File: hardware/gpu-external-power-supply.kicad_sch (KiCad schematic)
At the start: 0 parts

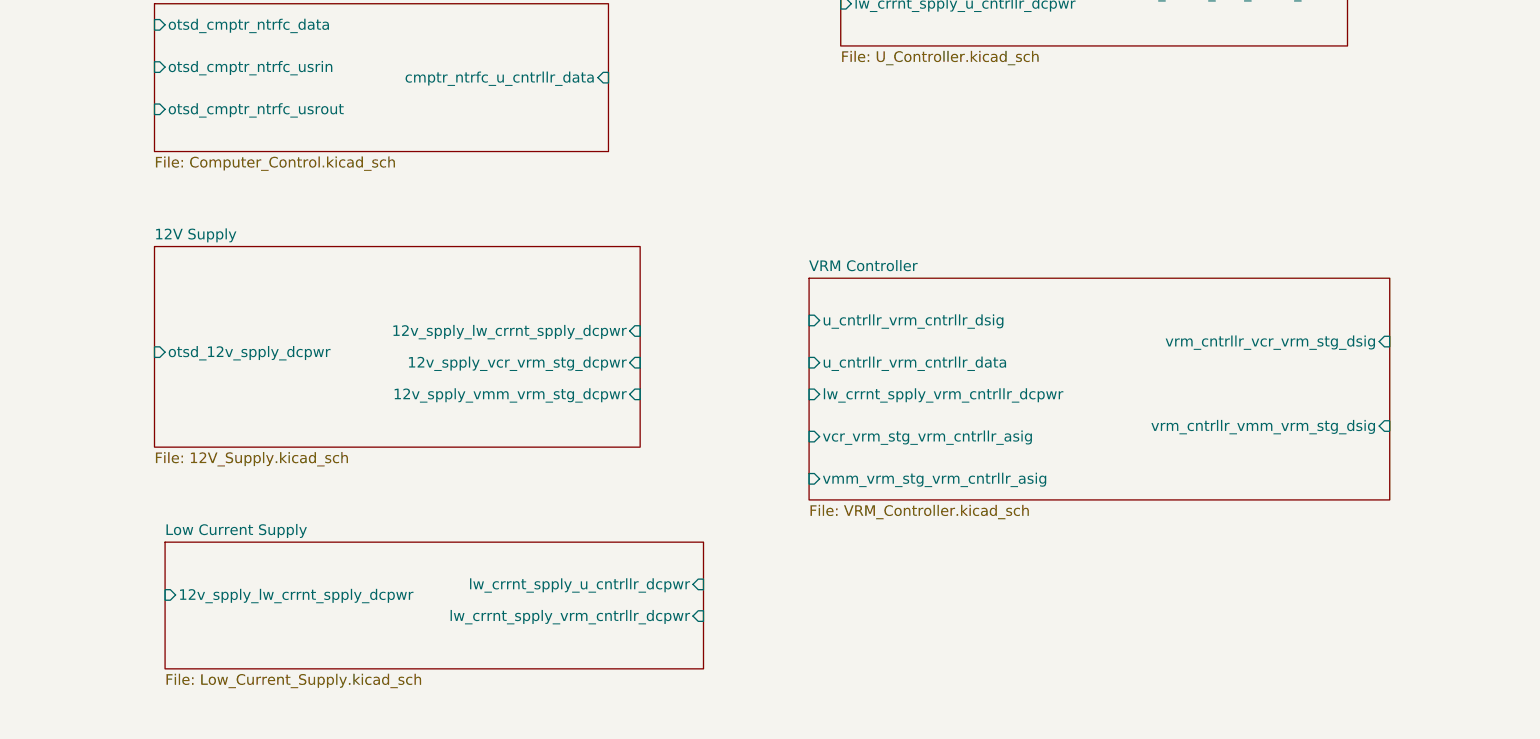
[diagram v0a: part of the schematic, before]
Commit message: refactor(schematic): Update VRM Controller Pins
Updated the VRM controller pinout on the main schematic
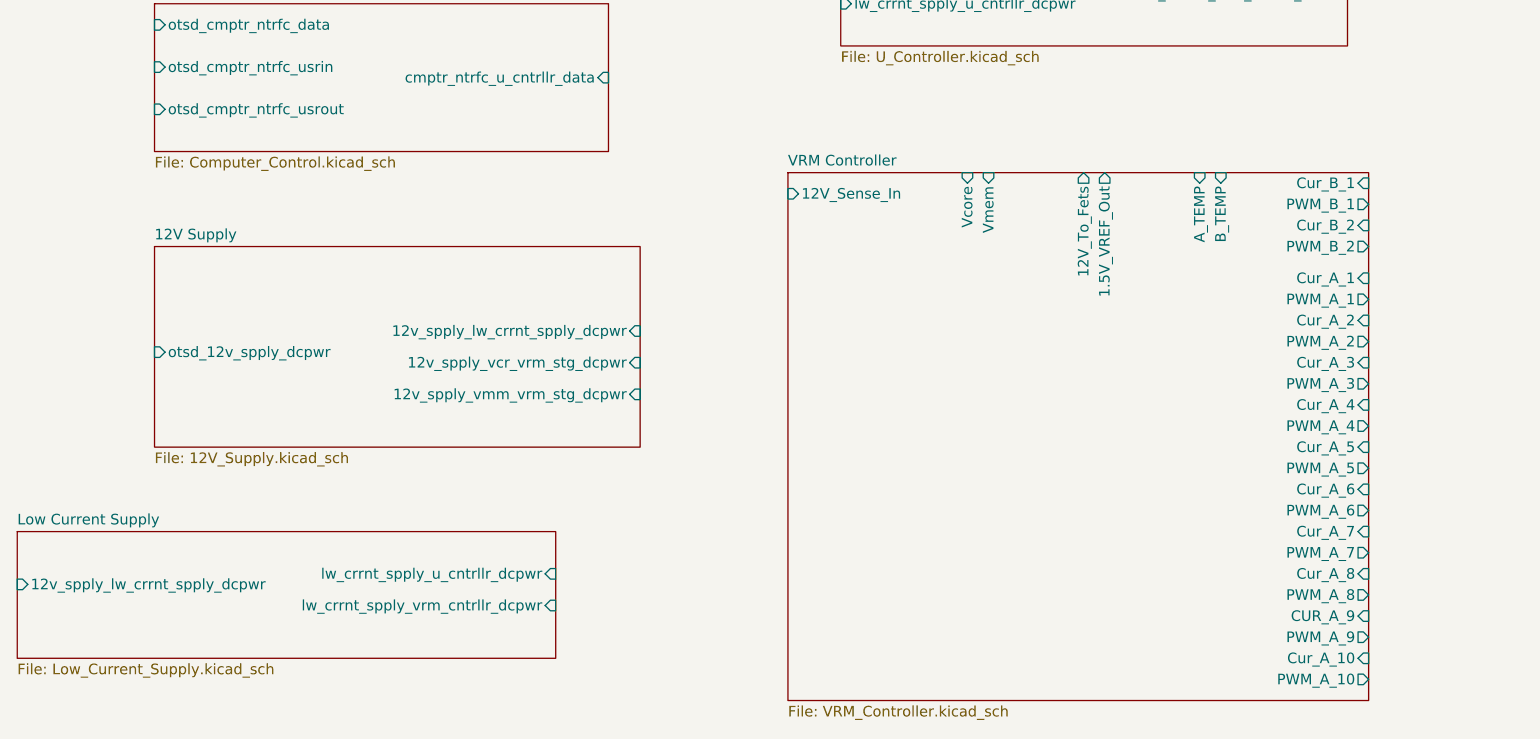
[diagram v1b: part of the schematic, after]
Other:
- sheet VRM Controller ports: added 1.5V_VREF_Out, 12V_Sense_In, 12V_To_Fets, A_TEMP, B_TEMP, CUR_A_9, Cur_A_1, Cur_A_10, Cur_A_2, Cur_A_3, Cur_A_4, Cur_A_5, Cur_A_6, Cur_A_7, Cur_A_8, Cur_B_1, Cur_B_2, PWM_A_1, PWM_A_10, PWM_A_2, PWM_A_3, PWM_A_4, PWM_A_5, PWM_A_6, PWM_A_7, PWM_A_8, PWM_A_9, PWM_B_1, PWM_B_2, Vcore, Vmem; removed lw_crrnt_spply_vrm_cntrllr_dcpwr, u_cntrllr_vrm_cntrllr_data, u_cntrllr_vrm_cntrllr_dsig, vcr_vrm_stg_vrm_cntrllr_asig, vmm_vrm_stg_vrm_cntrllr_asig, vrm_cntrllr_vcr_vrm_stg_dsig, vrm_cntrllr_vmm_vrm_stg_dsig

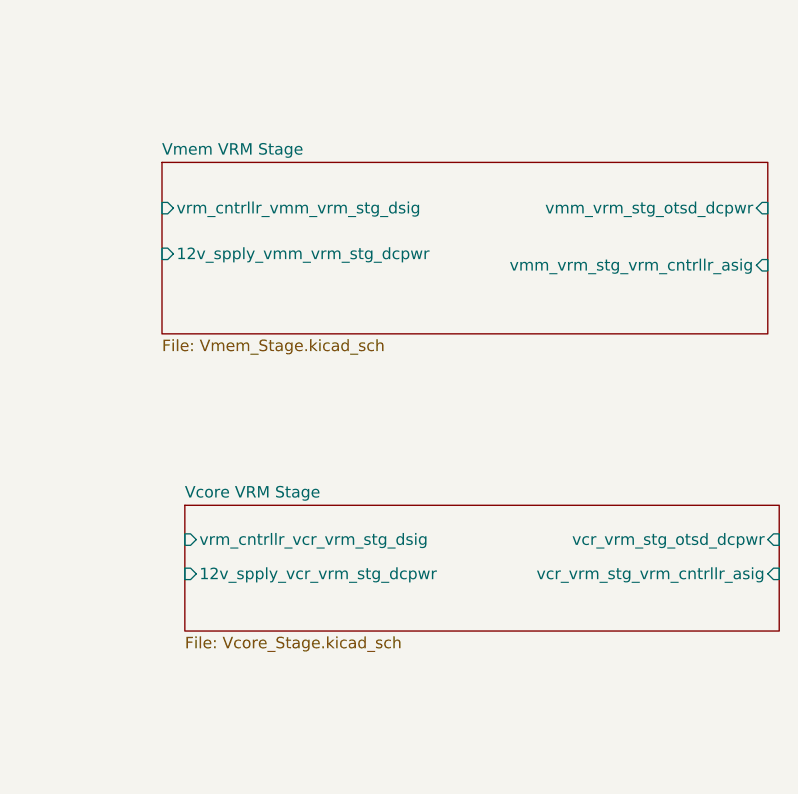
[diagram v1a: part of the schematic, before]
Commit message: rebase(schematic): Updated Vcore and Vmem pins
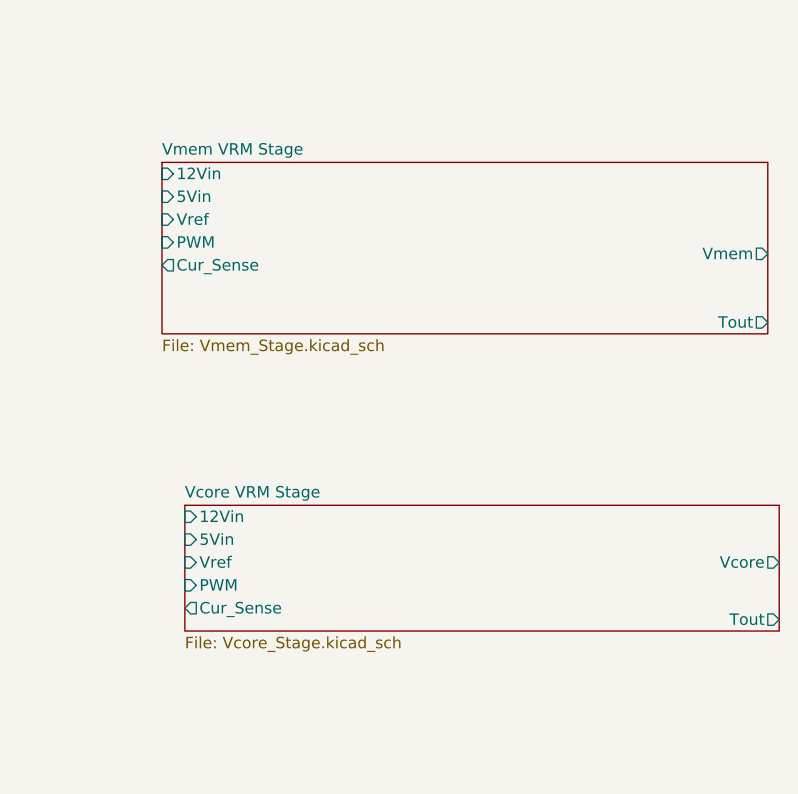
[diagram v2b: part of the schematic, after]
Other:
- sheet Vcore VRM Stage ports: added 12Vin, 5Vin, Cur_Sense, PWM, Tout, Vcore, Vref; removed 12v_spply_vcr_vrm_stg_dcpwr, vcr_vrm_stg_otsd_dcpwr, vcr_vrm_stg_vrm_cntrllr_asig, vrm_cntrllr_vcr_vrm_stg_dsig
- sheet Vmem VRM Stage ports: added 12Vin, 5Vin, Cur_Sense, PWM, Tout, Vmem, Vref; removed 12v_spply_vmm_vrm_stg_dcpwr, vmm_vrm_stg_otsd_dcpwr, vmm_vrm_stg_vrm_cntrllr_asig, vrm_cntrllr_vmm_vrm_stg_dsig
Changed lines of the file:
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@@
 			)
 		)
-		(pin "vrm_cntrllr_vmm_vrm_stg_dsig" input
-			(at 203.2 77.47 180)
-			(effects
-				(font
-					(size 1.27 1.27)
-				)
-				(justify left)
-			)
-		)
-		(pin "12v_spply_vmm_vrm_stg_dcpwr" input
-			(at 203.2 82.55 180)
-			(effects
-				(font
-					(size 1.27 1.27)
-				)
-				(justify left)
-			)
-		)
-		(pin "vmm_vrm_stg_otsd_dcpwr" input
-			(at 270.51 77.47 0)
-			(effects
-				(font
-					(size 1.27 1.27)
-				)
-				(justify right)
-			)
-		)
-		(pin "vmm_vrm_stg_vrm_cntrllr_asig" input
-			(at 270.51 83.82 0)
+		(pin "12Vin" input
+			(at 203.2 73.66 180)
+			(effects
+				(font
+					(size 1.27 1.27)
+				)
+				(justify left)
+			)
+		)
+		(pin "PWM" input
+			(at 203.2 81.28 180)
+			(effects
+				(font
+					(size 1.27 1.27)
+				)
+				(justify left)
+			)
+		)
+		(pin "Cur_Sense" output
+			(at 203.2 83.82 180)
+			(effects
+				(font
+					(size 1.27 1.27)
+				)
+				(justify left)
+			)
+		)
+		(pin "Vref" input
+			(at 203.2 78.74 180)
+			(effects
+				(font
+					(size 1.27 1.27)
+				)
+				(justify left)
+			)
+		)
+		(pin "5Vin" input
+			(at 203.2 76.2 180)
+			(effects
+				(font
+					(size 1.27 1.27)
+				)
+				(justify left)
+			)
+		)
+		(pin "Tout" output
+			(at 270.51 90.17 0)
+			(effects
+				(font
+					(size 1.27 1.27)
+				)
+				(justify right)
+			)
+		)
+		(pin "Vmem" output
+			(at 270.51 82.55 0)
 			(effects
 				(font
@@
 			)
 		)
-		(pin "vrm_cntrllr_vcr_vrm_stg_dsig" input
+		(pin "Vref" input
+			(at 205.74 116.84 180)
+			(effects
+				(font
+					(size 1.27 1.27)
+				)
+				(justify left)
+			)
+		)
+		(pin "Tout" output
+			(at 271.78 123.19 0)
+			(effects
+				(font
+					(size 1.27 1.27)
+				)
+				(justify right)
+			)
+		)
+		(pin "Cur_Sense" output
+			(at 205.74 121.92 180)
+			(effects
+				(font
+					(size 1.27 1.27)
+				)
+				(justify left)
+			)
+		)
+		(pin "5Vin" input
 			(at 205.74 114.3 180)
 			(effects
@@
 			)
 		)
-		(pin "12v_spply_vcr_vrm_stg_dcpwr" input
-			(at 205.74 118.11 180)
-			(effects
-				(font
-					(size 1.27 1.27)
-				)
-				(justify left)
-			)
-		)
-		(pin "vcr_vrm_stg_otsd_dcpwr" input
-			(at 271.78 114.3 0)
-			(effects
-				(font
-					(size 1.27 1.27)
-				)
-				(justify right)
-			)
-		)
-		(pin "vcr_vrm_stg_vrm_cntrllr_asig" input
-			(at 271.78 118.11 0)
-			(effects
-				(font
+		(pin "12Vin" input
+			(at 205.74 111.76 180)
+			(effects
+				(font
+					(size 1.27 1.27)
+				)
+				(justify left)
+			)
+		)
+		(pin "PWM" input
+			(at 205.74 119.38 180)
+			(effects
+				(font
+					(size 1.27 1.27)
+				)
+				(justify left)
+			)
+		)
+		(pin "Vcore" output
+			(at 271.78 116.84 0)
+			(effects
+				(font

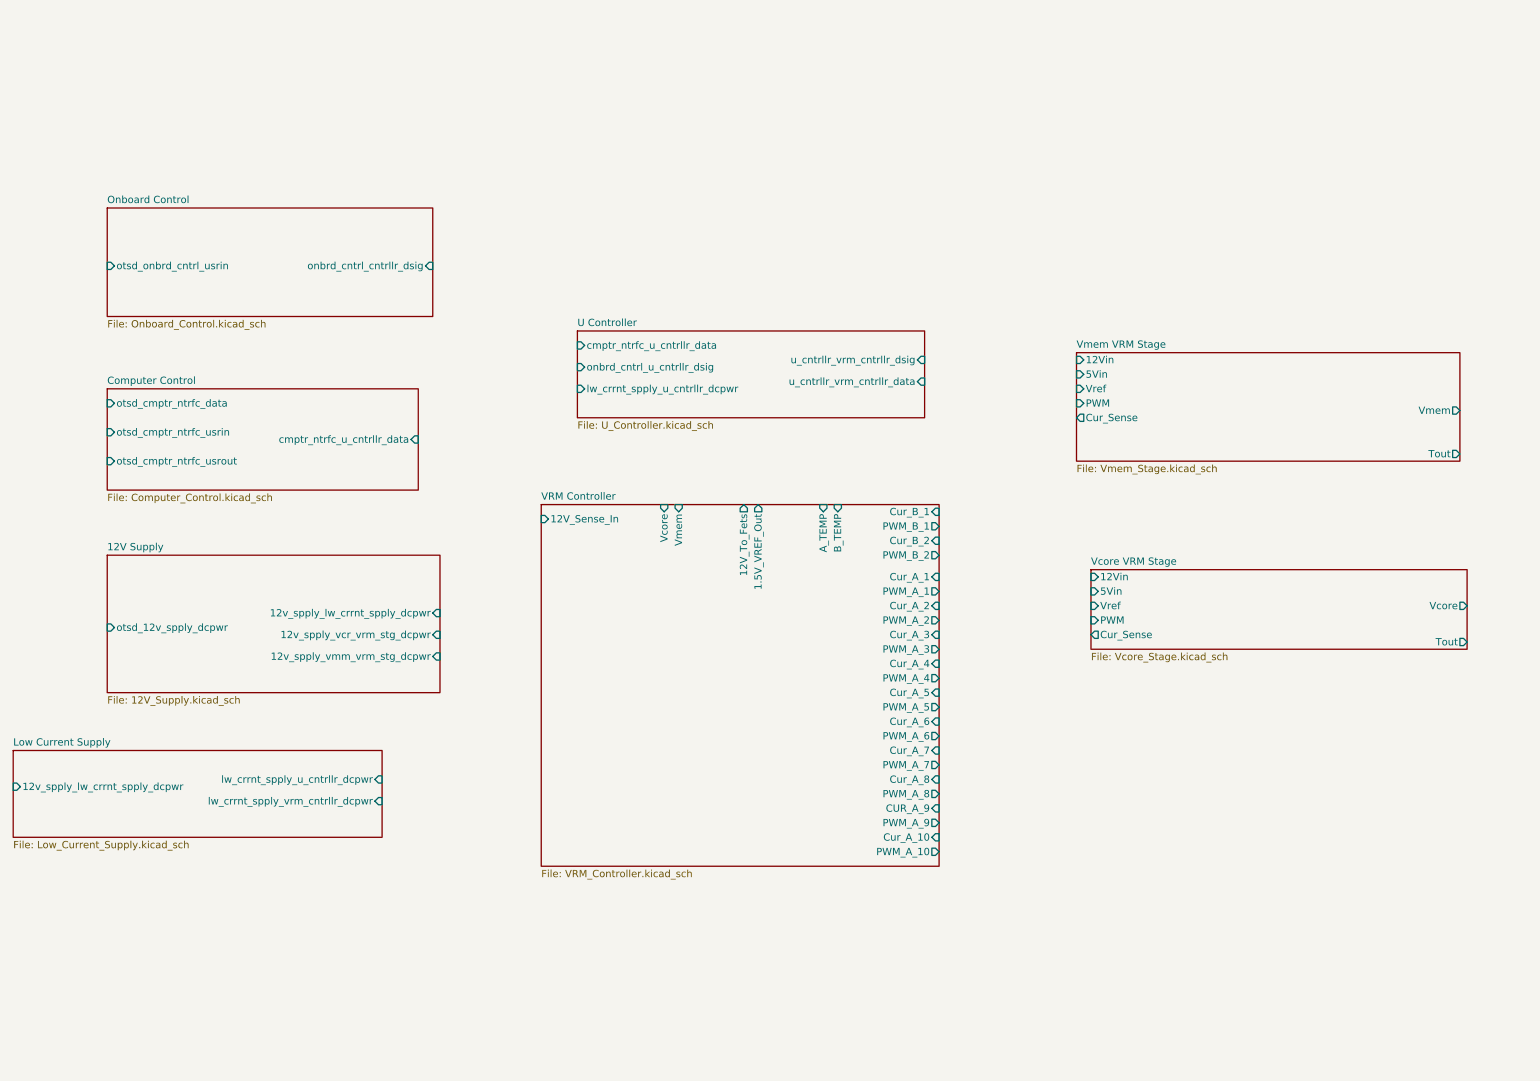
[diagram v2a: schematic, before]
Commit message: feat(schematic): Vmem schematic completed, connected controler and stages on main
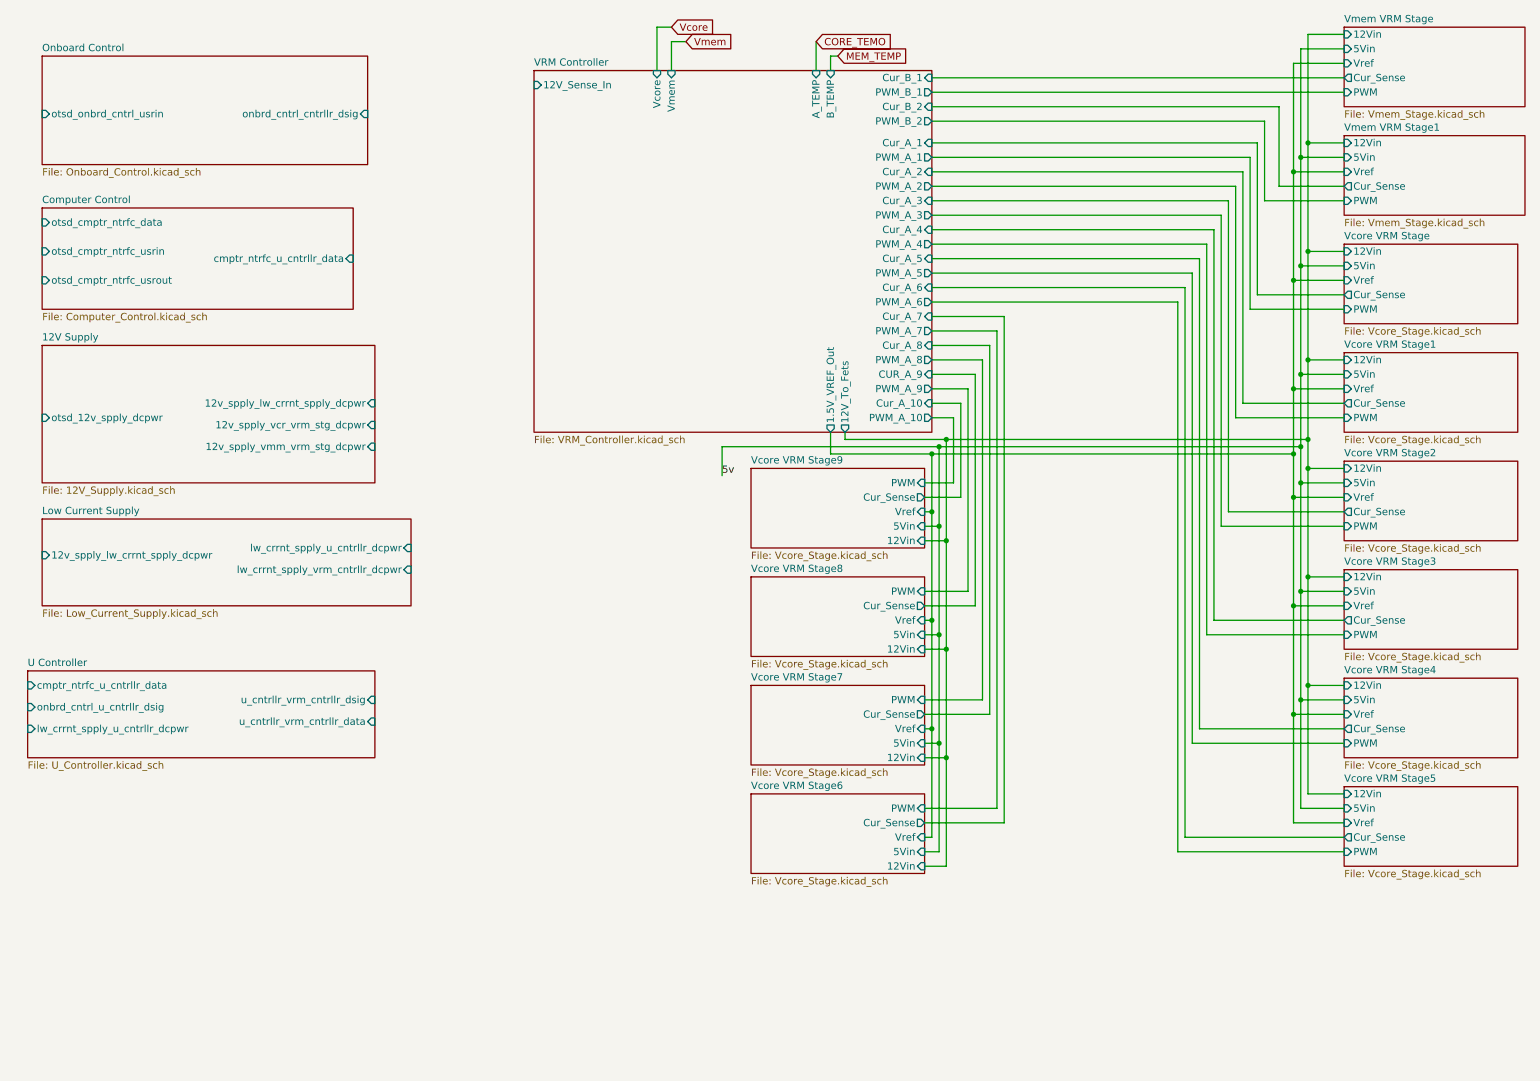
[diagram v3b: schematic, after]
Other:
- added sheet Vcore VRM Stage1 (Vcore_Stage.kicad_sch)
- added sheet Vcore VRM Stage2 (Vcore_Stage.kicad_sch)
- added sheet Vcore VRM Stage3 (Vcore_Stage.kicad_sch)
- added sheet Vcore VRM Stage4 (Vcore_Stage.kicad_sch)
- added sheet Vcore VRM Stage5 (Vcore_Stage.kicad_sch)
- added sheet Vcore VRM Stage6 (Vcore_Stage.kicad_sch)
- added sheet Vcore VRM Stage7 (Vcore_Stage.kicad_sch)
- added sheet Vcore VRM Stage8 (Vcore_Stage.kicad_sch)
- added sheet Vcore VRM Stage9 (Vcore_Stage.kicad_sch)
- added sheet Vmem VRM Stage1 (Vmem_Stage.kicad_sch)
- sheet Vcore VRM Stage ports: added none; removed Tout, Vcore
- sheet Vmem VRM Stage ports: added none; removed Tout, Vmem

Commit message: feat(PCB): Vrms for mem and core layed out
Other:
- sheet 12V Supply ports: added none; removed 12v_spply_lw_crrnt_spply_dcpwr, 12v_spply_vcr_vrm_stg_dcpwr, 12v_spply_vmm_vrm_stg_dcpwr
- sheet Low Current Supply ports: added none; removed 12v_spply_lw_crrnt_spply_dcpwr, lw_crrnt_spply_u_cntrllr_dcpwr, lw_crrnt_spply_vrm_cntrllr_dcpwr
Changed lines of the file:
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@@
-	(wire
-		(pts
-			(xy 140.97 88.9) (xy 140.97 93.98)
-		)
-		(stroke
-			(width 0)
-			(type default)
-		)
-	)
 	(wire
 		(pts
@@
 	(wire
 		(pts
-			(xy 179.07 88.9) (xy 140.97 88.9)
+			(xy 179.07 88.9) (xy 144.78 88.9)
 		)
 		(stroke
@@
 	(wire
 		(pts
+			(xy 101.6 25.4) (xy 107.95 25.4)
+		)
+		(stroke
+			(width 0)
+			(type default)
+		)
+	)
+	(wire
+		(pts
 			(xy 250.19 160.02) (xy 220.98 160.02)
 		)
@@
 			(width 0)
 			(type default)
-		)
-	)
-	(label "5v"
-		(at 140.97 93.98 0)
-		(fields_autoplaced yes)
-		(effects
-			(font
-				(size 1.27 1.27)
-			)
-			(justify left bottom)
 		)
 	)
@@
 		)
 	)
+	(global_label "5V"
+		(shape input)
+		(at 144.78 88.9 180)
+		(fields_autoplaced yes)
+		(effects
+			(font
+				(size 1.27 1.27)
+			)
+			(justify right)
+		)
+		(property "Intersheetrefs" "${INTERSHEET_REFS}"
+			(at 139.4967 88.9 0)
+			(effects
+				(font
+					(size 1.27 1.27)
+				)
+				(justify right)
+				(hide yes)
+			)
+		)
+	)
 	(global_label "Vmem"
 		(shape input)
@@
 		)
 	)
+	(global_label "12V"
+		(shape input)
+		(at 101.6 25.4 180)
+		(fields_autoplaced yes)
+		(effects
+			(font
+				(size 1.27 1.27)
+			)
+			(justify right)
+		)
+		(property "Intersheetrefs" "${INTERSHEET_REFS}"
+			(at 95.1072 25.4 0)
+			(effects
+				(font
+					(size 1.27 1.27)
+				)
+				(justify right)
+				(hide yes)
+			)
+		)
+	)
 	(sheet
 		(at 19.05 128.27)
@@
 			)
 		)
-		(pin "lw_crrnt_spply_u_cntrllr_dcpwr" input
-			(at 86.36 106.68 0)
-			(effects
-				(font
-					(size 1.27 1.27)
-				)
-				(justify right)
-			)
-		)
-		(pin "12v_spply_lw_crrnt_spply_dcpwr" input
-			(at 21.59 107.95 180)
-			(effects
-				(font
-					(size 1.27 1.27)
-				)
-				(justify left)
-			)
-		)
-		(pin "lw_crrnt_spply_vrm_cntrllr_dcpwr" input
-			(at 86.36 110.49 0)
-			(effects
-				(font
-					(size 1.27 1.27)
-				)
-				(justify right)
-			)
-		)
 		(instances
 			(project "gpu-external-power-supply"
@@
 			)
 		)
-		(pin "12v_spply_lw_crrnt_spply_dcpwr" input
-			(at 80.01 81.28 0)
-			(effects
-				(font
-					(size 1.27 1.27)
-				)
-				(justify right)
-			)
-		)
-		(pin "12v_spply_vcr_vrm_stg_dcpwr" input
-			(at 80.01 85.09 0)
-			(effects
-				(font
-					(size 1.27 1.27)
-				)
-				(justify right)
-			)
-		)
-		(pin "12v_spply_vmm_vrm_stg_dcpwr" input
-			(at 80.01 88.9 0)
-			(effects
-				(font
-					(size 1.27 1.27)
-				)
-				(justify right)
-			)
-		)
